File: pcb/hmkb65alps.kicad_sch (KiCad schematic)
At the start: 21 parts, among them J1 AVR-ISP-6, J2 USB4105GFA120, SW69 SW_Push, U1 ATmega32U4-A, Y1 16MHz

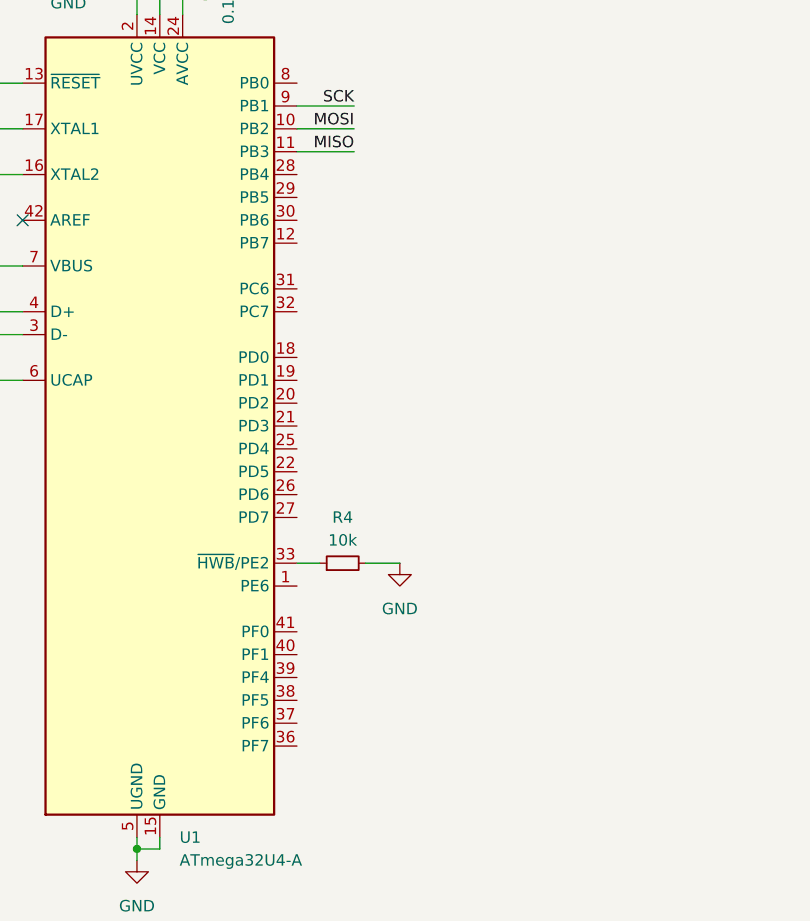
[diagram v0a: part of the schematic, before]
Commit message: route and assign all rows/columns of the matrix
also add some more vias where found neccessary
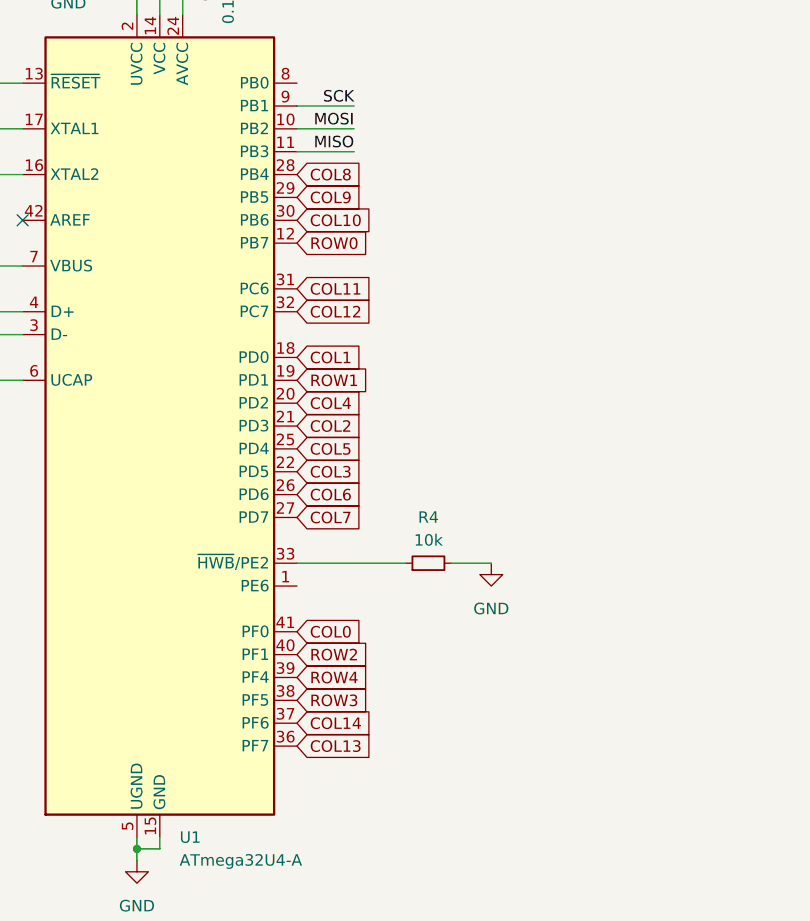
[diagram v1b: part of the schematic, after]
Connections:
- net ROW0: now reaches U1.12 (PB7)
- net COL1: now reaches U1.18 (PD0)
- net ROW1: now reaches U1.19 (PD1)
- net COL4: now reaches U1.20 (PD2)
- net COL2: now reaches U1.21 (PD3)
- net COL3: now reaches U1.22 (PD5)
- net COL5: now reaches U1.25 (PD4)
- net COL6: now reaches U1.26 (PD6)
- net COL7: now reaches U1.27 (PD7)
- net COL8: now reaches U1.28 (PB4)
- net COL9: now reaches U1.29 (PB5)
- net COL10: now reaches U1.30 (PB6)
- net COL11: now reaches U1.31 (PC6)
- net COL12: now reaches U1.32 (PC7)
- net COL13: now reaches U1.36 (PF7)
- net COL14: now reaches U1.37 (PF6)
- net ROW3: now reaches U1.38 (PF5)
- net ROW4: now reaches U1.39 (PF4)
- net ROW2: now reaches U1.40 (PF1)
- net COL0: now reaches U1.41 (PF0)
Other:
- moved on the sheet: R4
